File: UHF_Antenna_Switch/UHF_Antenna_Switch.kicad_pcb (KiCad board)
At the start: 2 copper layers, 10.7 x 19.8 mm, 36 parts, among them J1 Conn_N_Type_Female, J2 Conn_SO-239, J3 Conn_SMA_Female, J4 Screw_Terminal_01x02, K3 HF3-51, K4 HF3-51, Q2 2N7002, Q3 2N7002, SW1 SW_SP3T, U1 LTC5507ES6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

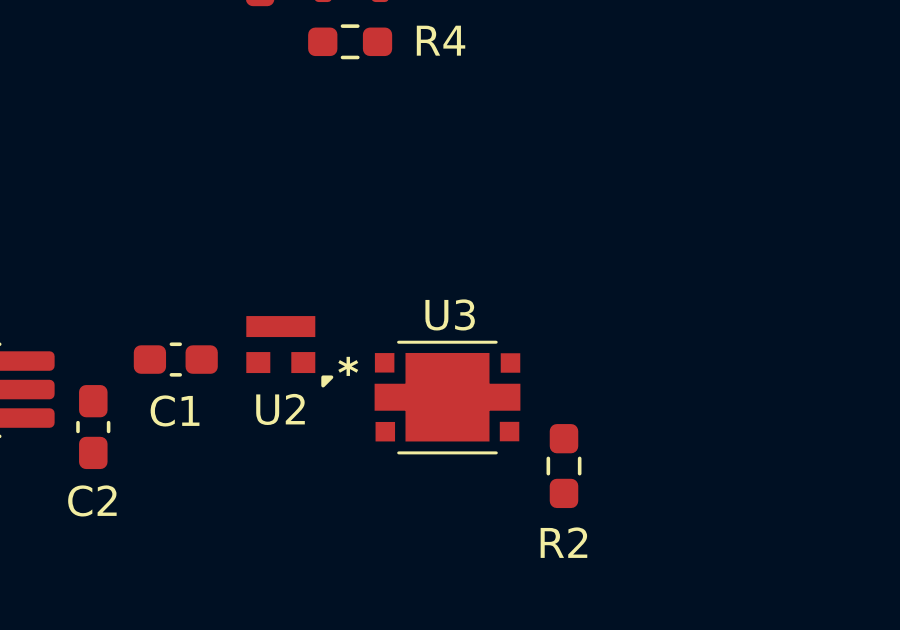
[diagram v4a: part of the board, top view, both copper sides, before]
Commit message: Configure net classes and trace widths
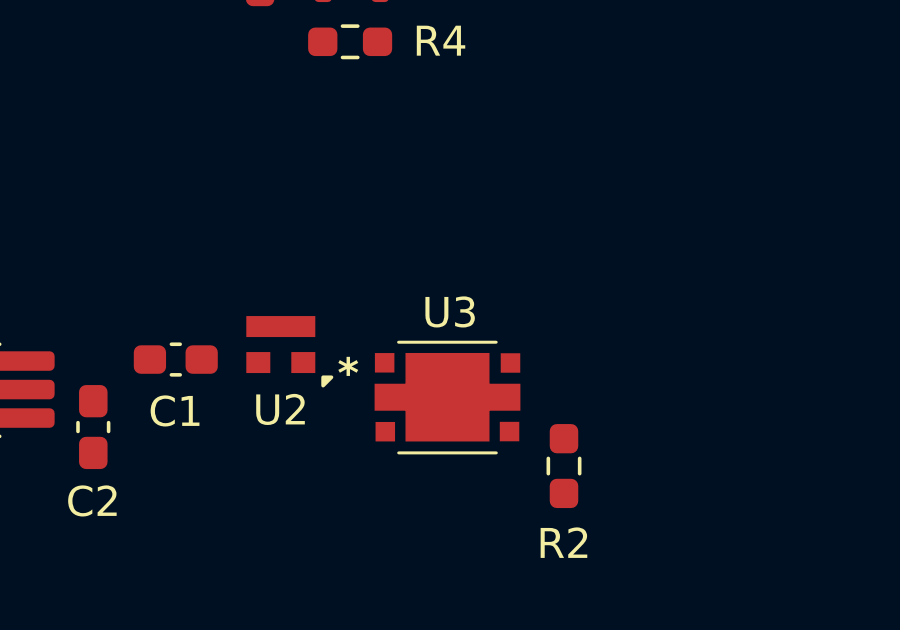
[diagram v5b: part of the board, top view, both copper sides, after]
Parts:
- U3: footprint 00-project-footprints:X4C09F1 - 30S -> 00-project-footprints:X4C09F1-30S
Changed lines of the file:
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@@
 	)
 	(setup
+		(stackup
+			(layer "F.SilkS"
+				(type "Top Silk Screen")
+			)
+			(layer "F.Paste"
+				(type "Top Solder Paste")
+			)
+			(layer "F.Mask"
+				(type "Top Solder Mask")
+				(thickness 0.01)
+			)
+			(layer "F.Cu"
+				(type "copper")
+				(thickness 0.035)
+			)
+			(layer "dielectric 1"
+				(type "core")
+				(thickness 1.51)
+				(material "FR4")
+				(epsilon_r 4.5)
+				(loss_tangent 0.02)
+			)
+			(layer "B.Cu"
+				(type "copper")
+				(thickness 0.035)
+			)
+			(layer "B.Mask"
+				(type "Bottom Solder Mask")
+				(thickness 0.01)
+			)
+			(layer "B.Paste"
+				(type "Bottom Solder Paste")
+			)
+			(layer "B.SilkS"
+				(type "Bottom Silk Screen")
+			)
+			(copper_finish "None")
+			(dielectric_constraints no)
+		)
 		(pad_to_mask_clearance 0)
 		(allow_soldermask_bridges_in_footprints no)
@@
 		(capping no)
 		(filling no)
+		(zone_defaults)
 		(pcbplotparams
 			(layerselection 0x00000000_00000000_55555555_5755f5ff)
@@
 		)
 	)
-	(footprint "00-project-footprints:X4C09F1 - 30S"
+	(footprint "00-project-footprints:X4C09F1-30S"
 		(layer "F.Cu")
 		(at 97.378151 98.941598)
+		(descr "30 dB Directional RF Coupler")
 		(property "Reference" "U3"
-			(at 0 -0.4 0)
+			(at 0 -0.5 0)
 			(unlocked yes)
 			(layer "F.SilkS")
@@
 				(font
 					(size 1 1)
-					(thickness 0.15)
+					(thickness 0.1)
 				)
 			)

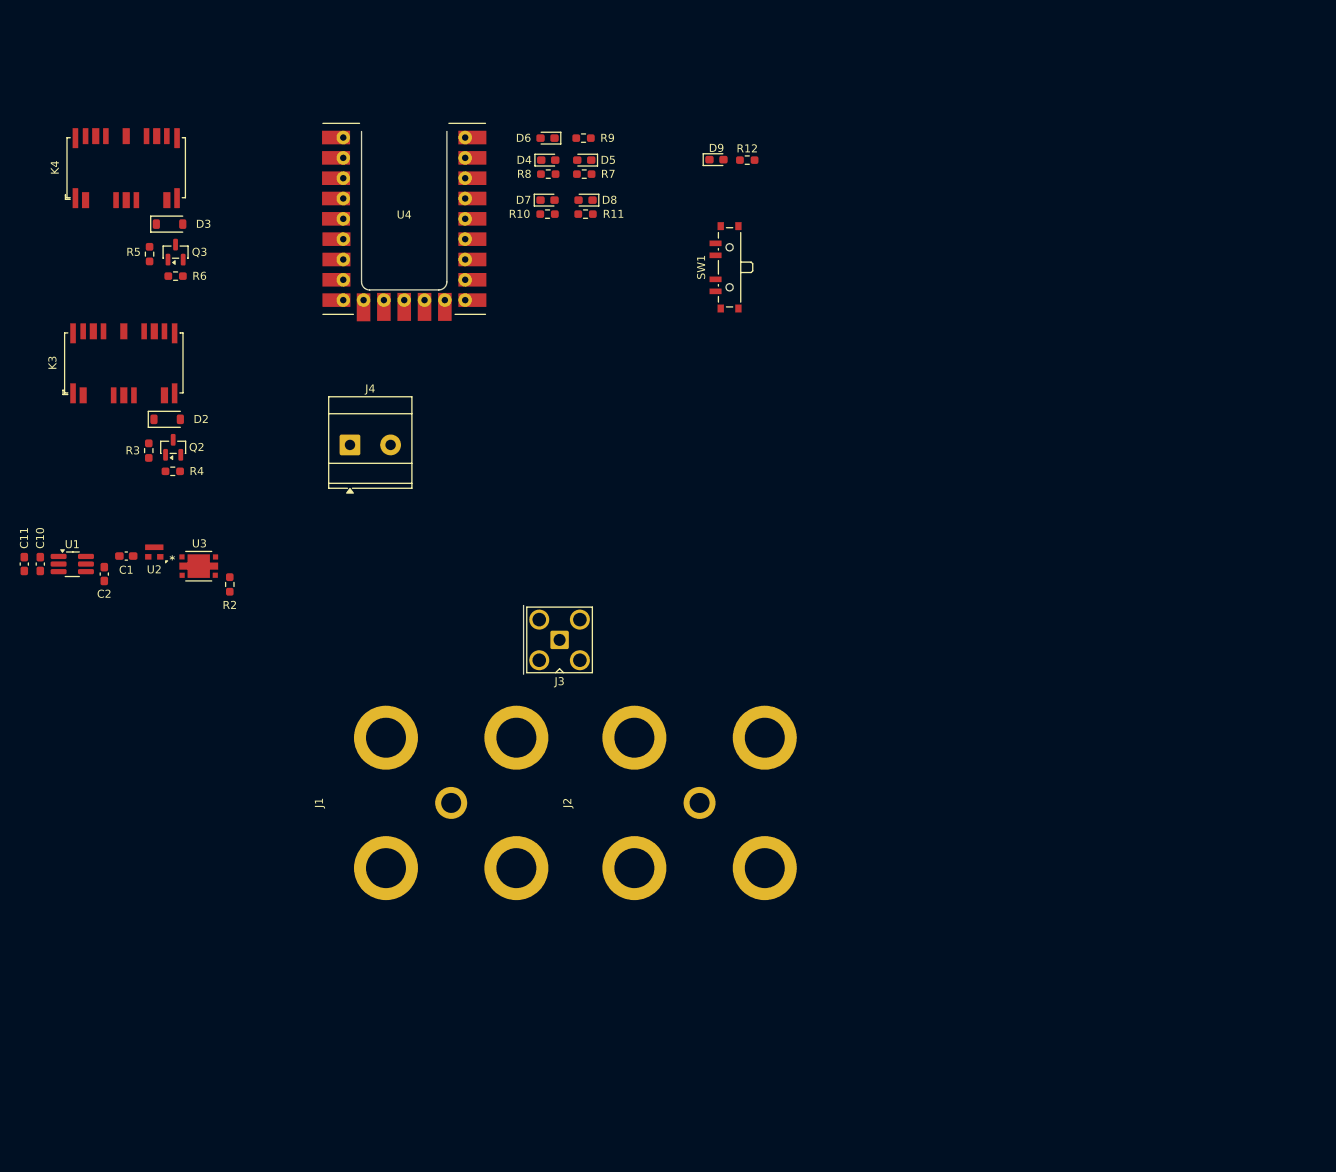
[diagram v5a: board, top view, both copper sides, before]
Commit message: Complete initial positioning of components (no routing)
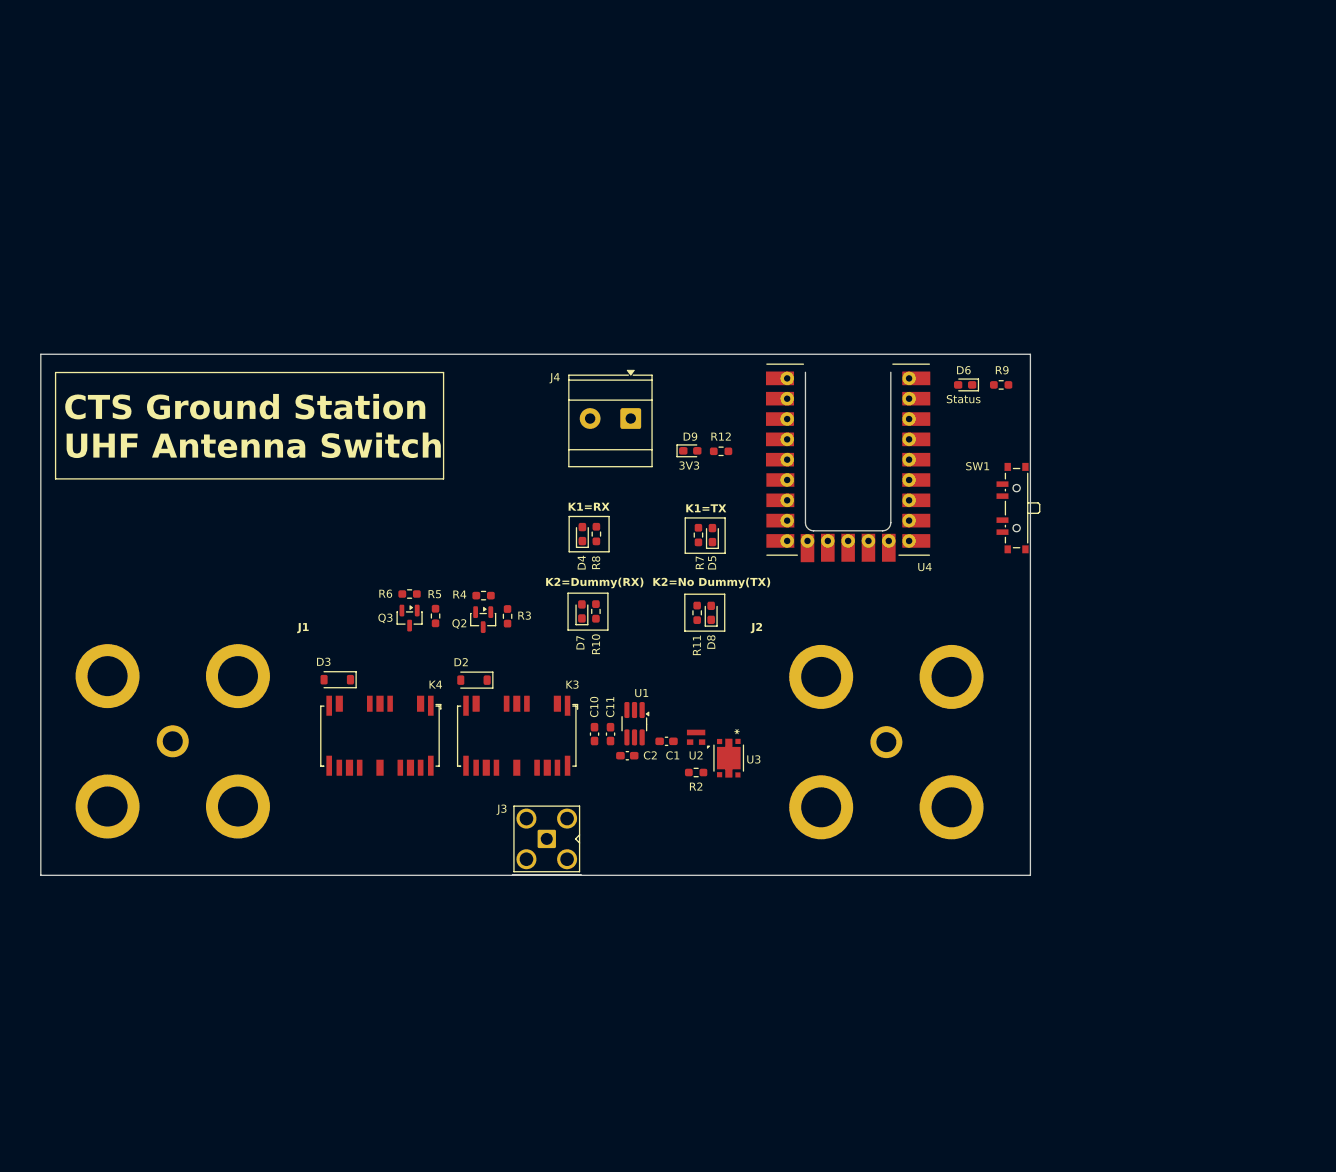
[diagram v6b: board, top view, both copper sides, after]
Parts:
- moved K4 77.7 mm to (120.0, 122.5), turned to -90 degrees
- moved C11 76.3 mm to (148.8, 122.2), turned to 90 degrees
- moved U3 73.4 mm to (165.9, 125.3), turned to -90 degrees
- moved U1 73.1 mm to (151.8, 121.0), turned to -90 degrees
- moved C10 72.5 mm to (146.8, 122.2), turned to 90 degrees
- moved U2 71.6 mm to (159.5, 122.7)
- moved C1 71.4 mm to (155.8, 123.2)
- moved C2 69.2 mm to (150.9, 125.0), turned to 0 degrees
- moved K3 67.7 mm to (137.1, 122.5), turned to -90 degrees
- moved U4 63.1 mm to (168.3, 100.8)
- moved R2 62.9 mm to (159.5, 127.0), turned to 180 degrees
- moved D3 60.7 mm to (114.6, 115.5), turned to 180 degrees
- moved D6 60.6 mm to (193.1, 78.6)
- moved R9 60.6 mm to (197.6, 78.6)
- moved R5 57.7 mm to (126.9, 107.5), turned to 90 degrees
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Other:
- board size 10.7 x 19.8 mm -> 123.7 x 65.1 mm
- board text added: "3V3"
- board text added: "CTS Ground Station UHF Antenna Switch"
- board text added: "K1=RX"
- board text added: "K1=TX"
- board text added: "K2=Dummy(RX)"
- board text added: "K2=No Dummy(TX)"
- board text added: "Status"

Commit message: Schematic: Add PTT switches, PTT header, 5V power screw
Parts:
- added J4: Screw_Terminal_01x04, TerminalBlock_Phoenix:TerminalBlock_Phoenix_MKDS-1,5-4-5.08_1x04_P5.08mm_Horizontal, F.Cu at (86.1, 53.2)
- added J5: Conn_02x03_Odd_Even, Connector_PinHeader_2.54mm:PinHeader_2x03_P2.54mm_Vertical, F.Cu at (95.3, 61.4)
- added R13: 5k1, Resistor_SMD:R_0603_1608Metric_Pad0.98x0.95mm_HandSolder, F.Cu at (102.4, 60.4)
- added R14: 5k1, Resistor_SMD:R_0603_1608Metric_Pad0.98x0.95mm_HandSolder, F.Cu at (102.4, 62.9)
- added SW2: SW_Push, Button_Switch_THT:SW_PUSH_6mm_H4.3mm, F.Cu at (84.5, 61.1)
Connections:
- SW1 pad 1: Net-(U4-GP6) -> Net-(U4-GP8)
- SW1 pad 4: Net-(U4-GP8) -> Net-(U4-GP6)
- U4 pad 1: unconnected-(U4-5V-Pad1) -> +5V
- U4 pad 11: TX_EN_RELAY_K1 -> unconnected-(U4-GP1-Pad11)_1
- U4 pad 12: TX_EN_RELAY_K2 -> PTT_INPUT_1
- U4 pad 13: unconnected-(U4-GP3-Pad13) -> PTT_INPUT_2
- U4 pad 5: unconnected-(U4-GP28-Pad5) -> TX_EN_RELAY_K1
- U4 pad 6: unconnected-(U4-GP27-Pad6) -> TX_EN_RELAY_K2

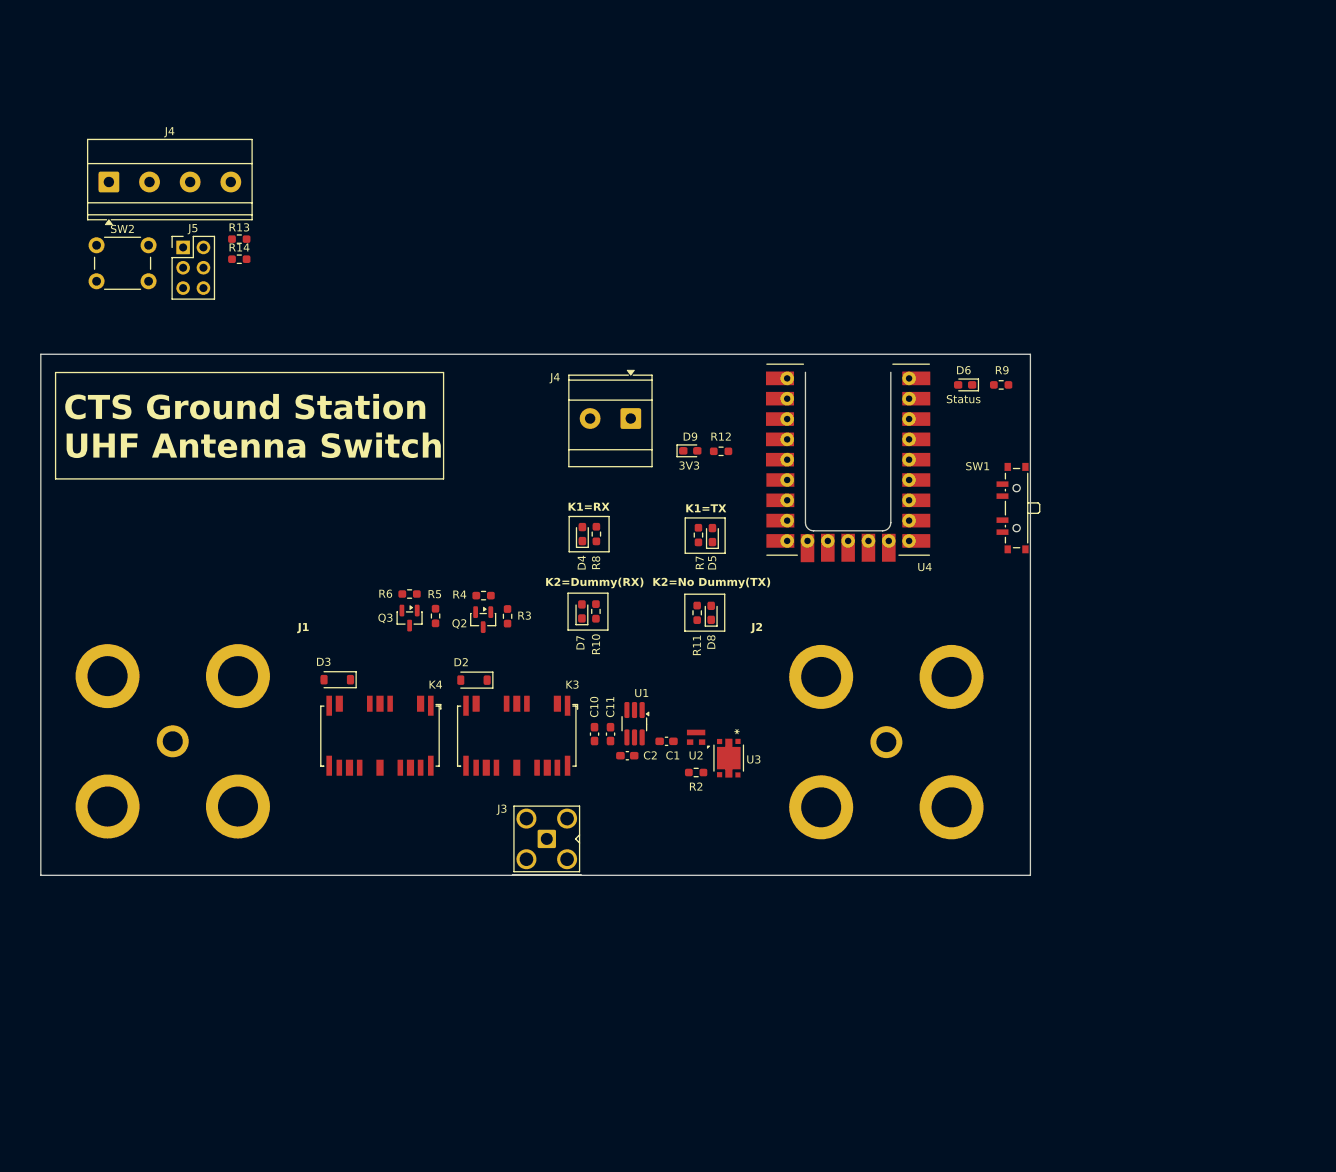
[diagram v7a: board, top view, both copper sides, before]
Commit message: Footprint: Draw RF coupler with microstrip
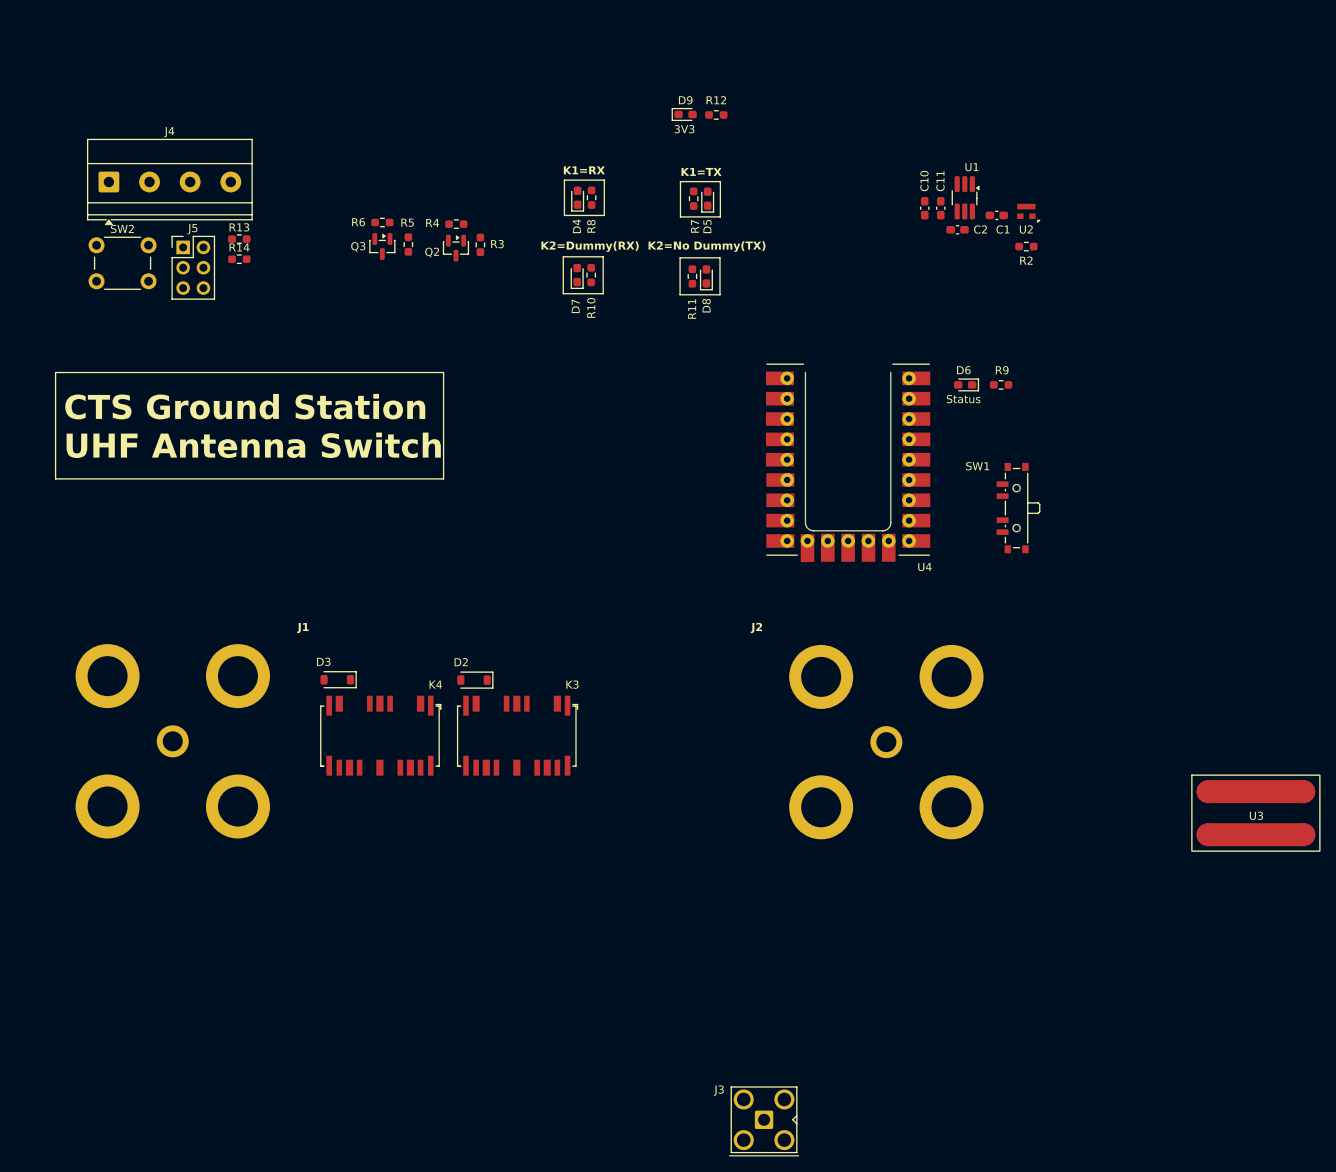
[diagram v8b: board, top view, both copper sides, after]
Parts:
- removed the J4 at (151.3, 82.8)
- U3: value X4C09F1-30S -> PCB-Trace-RF-Coupler; footprint 00-project-footprints:X4C09F1-30S -> 00-project-footprints:PCB-Trace-RF-Coupler
- moved C1 77.6 mm to (197.1, 57.4)
- moved C10 77.6 mm to (188.1, 56.5)
- moved C11 77.6 mm to (190.1, 56.5)
- moved C2 77.6 mm to (192.2, 59.2)
- moved R2 77.6 mm to (200.8, 61.3)
- moved U1 77.6 mm to (193.1, 55.2)
- moved U2 77.6 mm to (200.8, 56.9)
- moved U3 63.8 mm to (229.4, 130.9), turned to 0 degrees
- moved R3 46.6 mm to (132.5, 61.1)
- moved Q2 46.6 mm to (129.4, 61.5)
- moved Q3 46.6 mm to (120.2, 61.3)
- moved R4 46.6 mm to (129.5, 58.5)
- moved R5 46.6 mm to (123.5, 61.0)
- moved R6 46.6 mm to (120.2, 58.3)
- moved J3 44.4 mm to (168.0, 170.5)
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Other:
- board size 123.7 x 65.1 mm -> 10.7 x 19.8 mm
